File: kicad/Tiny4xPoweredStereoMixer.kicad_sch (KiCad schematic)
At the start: 42 parts, among them J1 AudioJack3_SwitchTR, J2 AudioJack3_SwitchTR, J3 AudioJack3_SwitchTR, J4 AudioJack3_SwitchTR, J9 AudioJack3_SwitchTR, U1 TL072, U2 TL072

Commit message: updated main
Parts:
- removed TP1: TestPoint, TestPoint:TestPoint_Keystone_5005-5009_Compact, symbol Connector:TestPoint
- added H3, H4: MountingHole, MountingHole:MountingHole_2.7mm_M2.5, symbol Mechanical:MountingHole
- C10, C11, C12, C14, C17, C18, C5, C7: now not fitted; now left out of the parts list
- C19, C20: footprint Capacitor_SMD:C_1210_3225Metric_Pad1.33x2.70mm_HandSolder -> Capacitor_SMD:C_0805_2012Metric_Pad1.18x1.45mm_HandSolder; now not fitted; now left out of the parts list
- H1, H2: footprint MountingHole:MountingHole_3mm -> MountingHole:MountingHole_2.7mm_M2.5
- RV1, RV2, RV3, RV4: Mouser 688-RK12L1210C1K -> 688-RK12L12A0C0R
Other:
- removed sheet PowerSupply
- added sheet TPS54202 Inverting PSU (tps54202_inverting_psu.kicad_sch)
- note added: "Bridge unless populated if AC coupling is needed"
- company: (none) -> Created By: ${AUTHOR}
- title: (none) -> ${PROJECTNAME}
- moved on the sheet: R12, R14

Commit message: PSU now uses +/- 2.5V; Added barrel jack; updated layout
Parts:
- removed C10, C11, C12, C14, C17, C18, C5, C7: 100nF, Capacitor_SMD:C_0603_1608Metric_Pad1.08x0.95mm_HandSolder, symbol Device:C
- removed C19, C20: 10uF, Capacitor_SMD:C_0805_2012Metric_Pad1.18x1.45mm_HandSolder, symbol Device:C
- added J6: Barrel_Jack_Switch, Connector_BarrelJack:BarrelJack_Horizontal, symbol Connector:Barrel_Jack_Switch
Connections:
- net GND: now also J6.2, J6.3
- net at J2.T: now also RV2.6
- net at R10.2, U1.7: now also J9.R
- net at J4.R: now also RV4.3
- net at J4.T: now also RV4.6
- net at RV1.3: now also J1.R
- net at R15.2, U2.7: now also J9.T
- net at RV2.3: now also J2.R
- net at J3.T: now also RV3.6
- net at RV1.6: now also J1.T
- net at J3.R: now also RV3.3
- net +12V renamed +2V5
- net -12V renamed -2V5
- new net +5V: J6.1
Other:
- added sheet LM1117 Low Dropout Regulator (lm1117_ldo.kicad_sch)
- sheet TPS54202 Inverting PSU ports: added smps_in, smps_out; removed none
- note added: "Min input for TPS54202 = 4.5V"
- moved on the sheet: C13, C6, C8, C9, H1, H2, H3, H4, J1, J2, J3, J4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

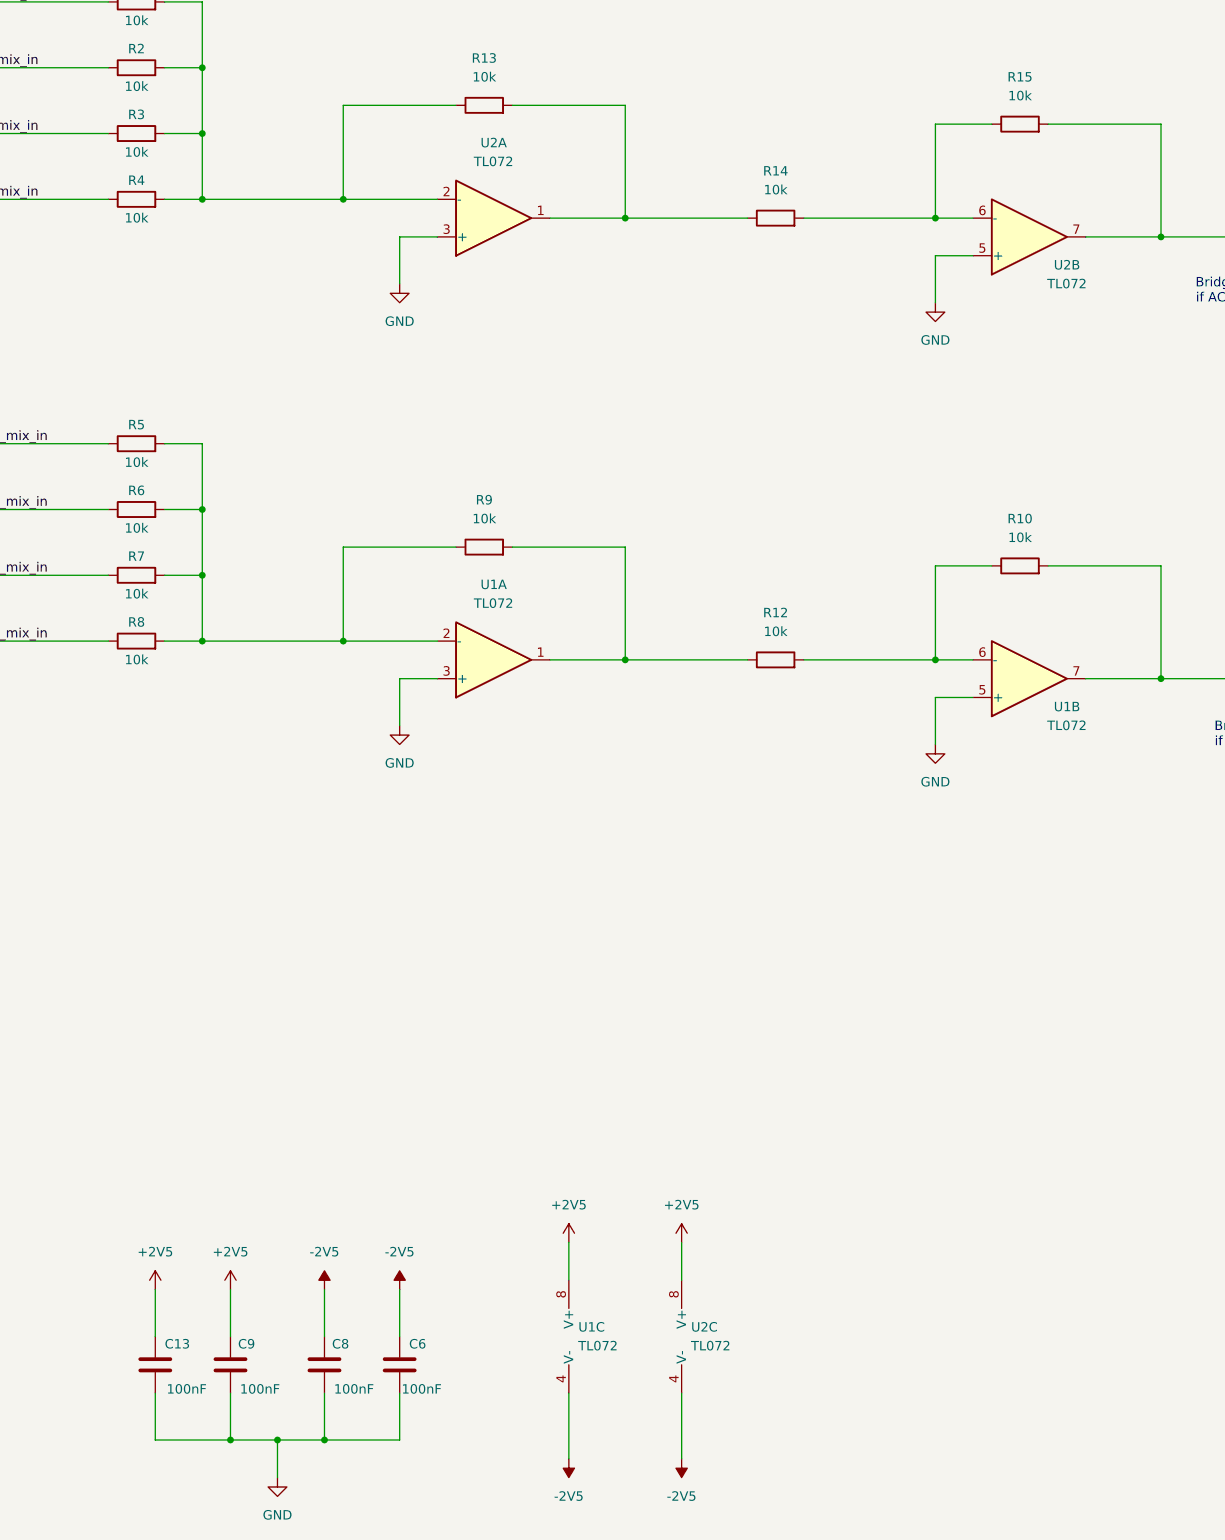
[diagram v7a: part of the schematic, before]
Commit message: Created missing SOT-23-THIN-14 footprint; Replaced 2xTL072 with 1xTL074; updated layout
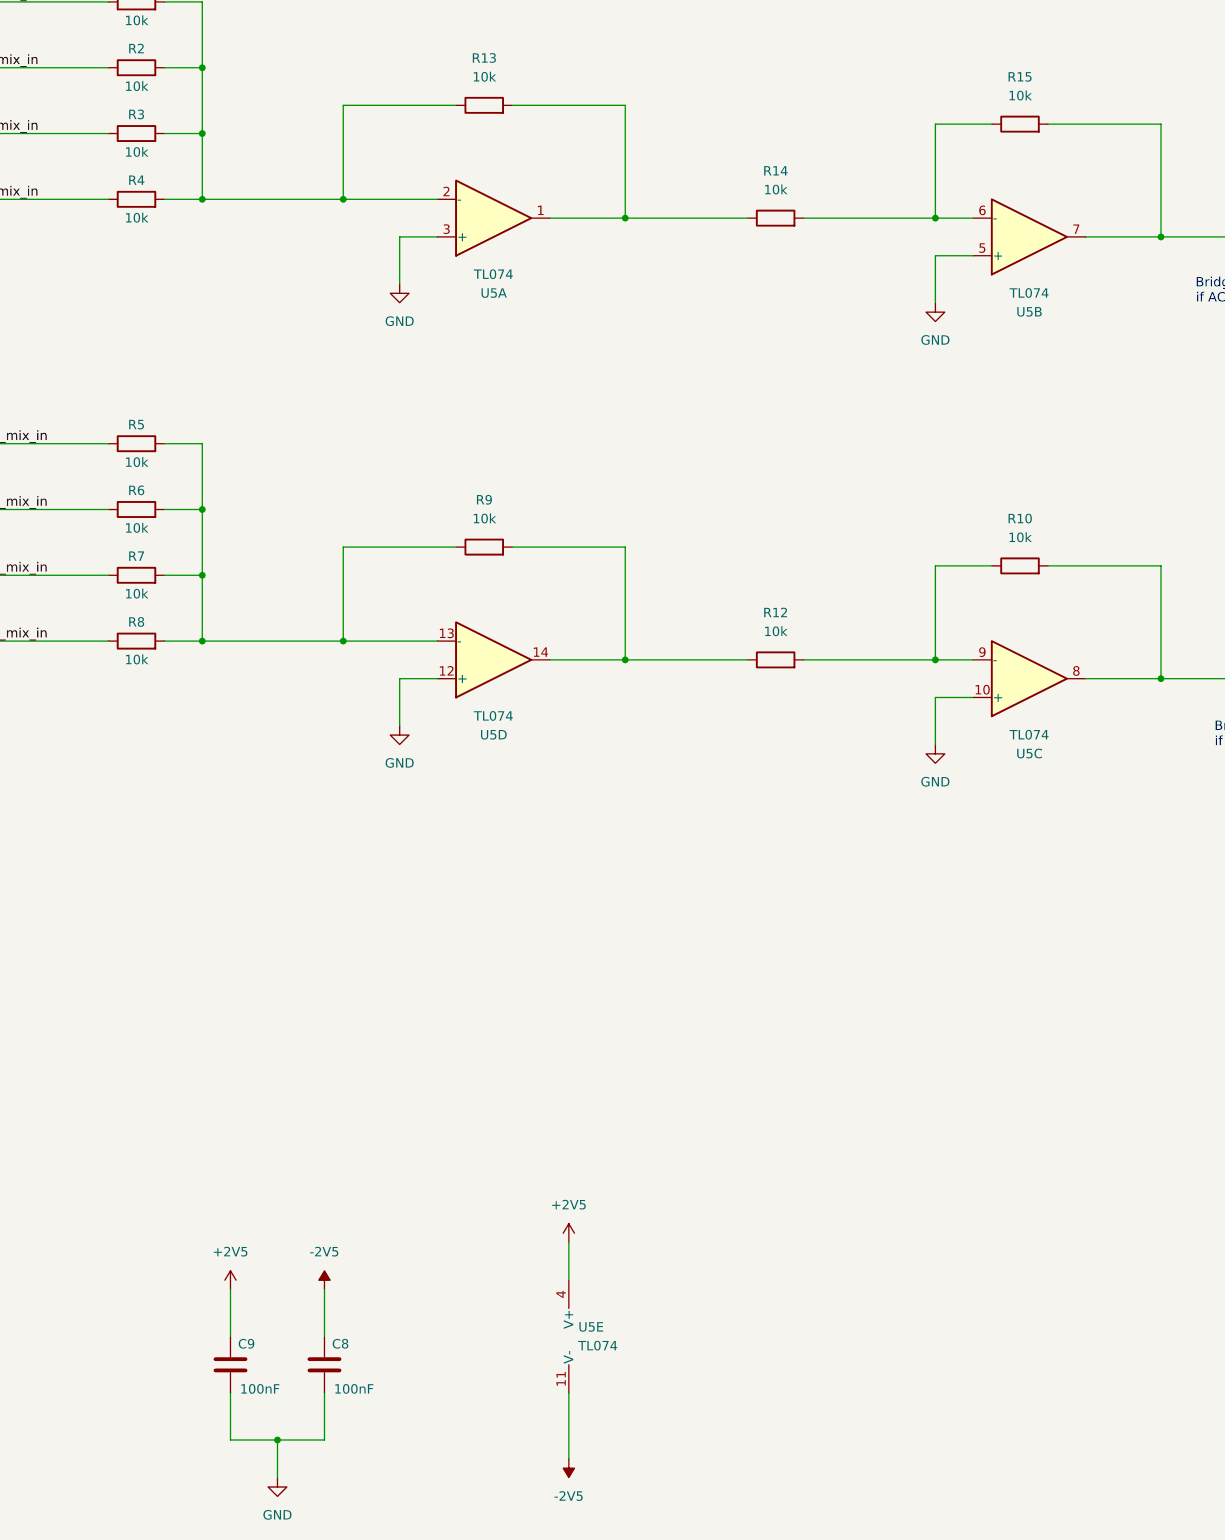
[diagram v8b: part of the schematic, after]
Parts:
- removed C13, C6: 100nF, Capacitor_SMD:C_0603_1608Metric_Pad1.08x0.95mm_HandSolder, symbol Device:C
- removed U1, U2: TL072, Package_SO:SOIC-8_3.9x4.9mm_P1.27mm, symbol Amplifier_Operational:TL072
- added U5: TL074, SOT-23-THIN-14:SOIC-14, symbol Amplifier_Operational:TL074
- C8, C9: footprint Capacitor_SMD:C_0603_1608Metric_Pad1.08x0.95mm_HandSolder -> Capacitor_SMD:C_0402_1005Metric_Pad0.74x0.62mm_HandSolder
- R1, R10, R12, R13, R14, R15, R2, R3, R4, R5, R6, R7, R8, R9: footprint Resistor_SMD:R_0805_2012Metric_Pad1.20x1.40mm_HandSolder -> Resistor_SMD:R_0402_1005Metric_Pad0.72x0.64mm_HandSolder
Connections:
- net +2V5: now also U5.4 (V+)
- net -2V5: now also U5.11 (V-)
- net GND: now also U5.10 (+), U5.12 (+), U5.3 (+), U5.5 (+)
- net at R10.1, R12.2: now also U5.9 (-)
- net at J9.R, R10.2: now also U5.8
- net at R13.2, R14.1: now also U5.1
- net at R14.2, R15.1: now also U5.6 (-)
- net at R1.2, R13.1, R2.2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: now also U5.2 (-)
- net at R12.1, R9.2: now also U5.14
- net at R5.2, R6.2, R7.2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: now also U5.13 (-)
- net at J9.T, R15.2: now also U5.7
